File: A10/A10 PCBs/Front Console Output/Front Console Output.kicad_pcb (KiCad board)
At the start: 2 copper layers, 99.8 x 99.5 mm, 43 parts, among them J1 STEPPER_9, J10 STEPPER_5, J11 STEPPER_6, J13 STEPPER_7, J17 STEPPER_8, J2 STEPPER_1, J20 8_MS2, J24 STEPPER_10, J25 STEPPER_11, J26 STEPPER_12, J27 STEPPER_13, J3 STEPPER_2, J41 PWM, J42 Communication, J43 Analog, J44 Analog, J45 Power, J5 STEPPER_3, J6 STEPPER_4, J7 STEPPER IN 12-20VDC, P1 Power, P2 Analog, P3 Analog, P4 Digital, P5 PWM, P6 PWM, P7 Communication, P8 PWM, U1 USR-ES1

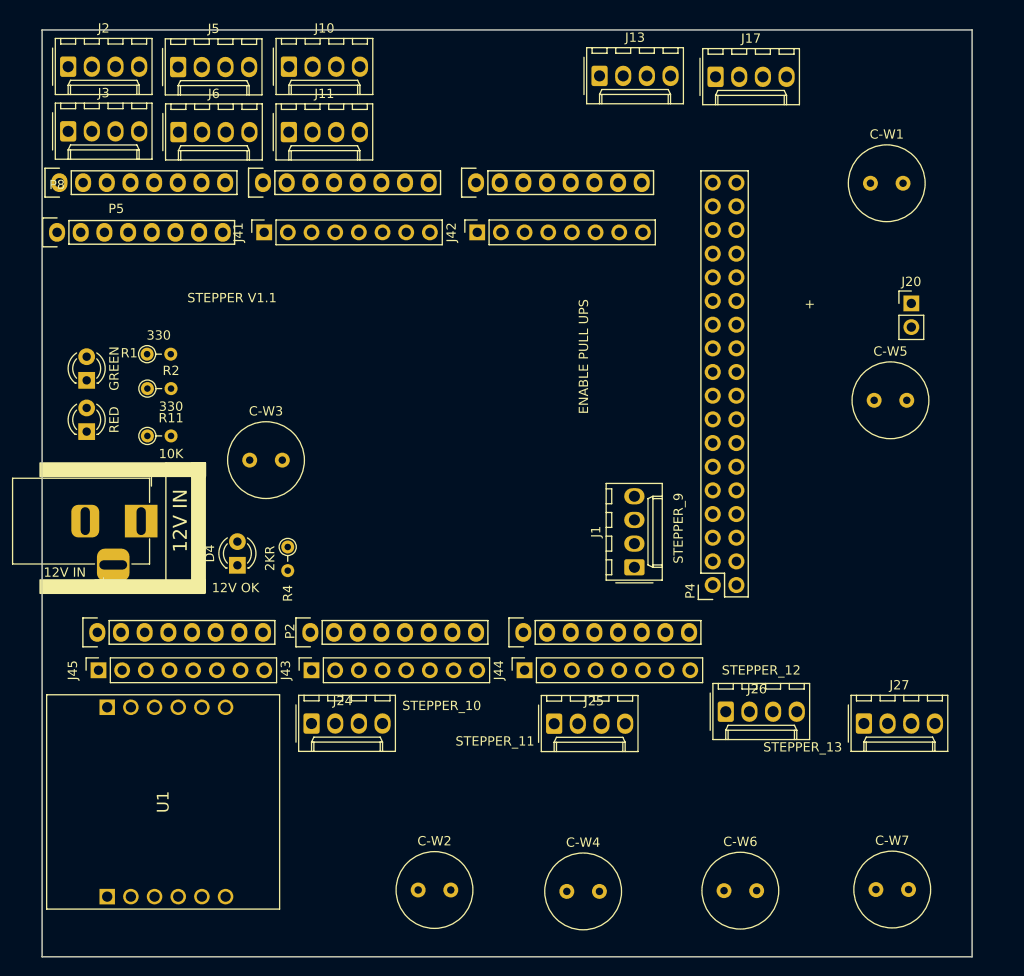
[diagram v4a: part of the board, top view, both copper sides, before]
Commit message: Refreshed Front Console Steppers
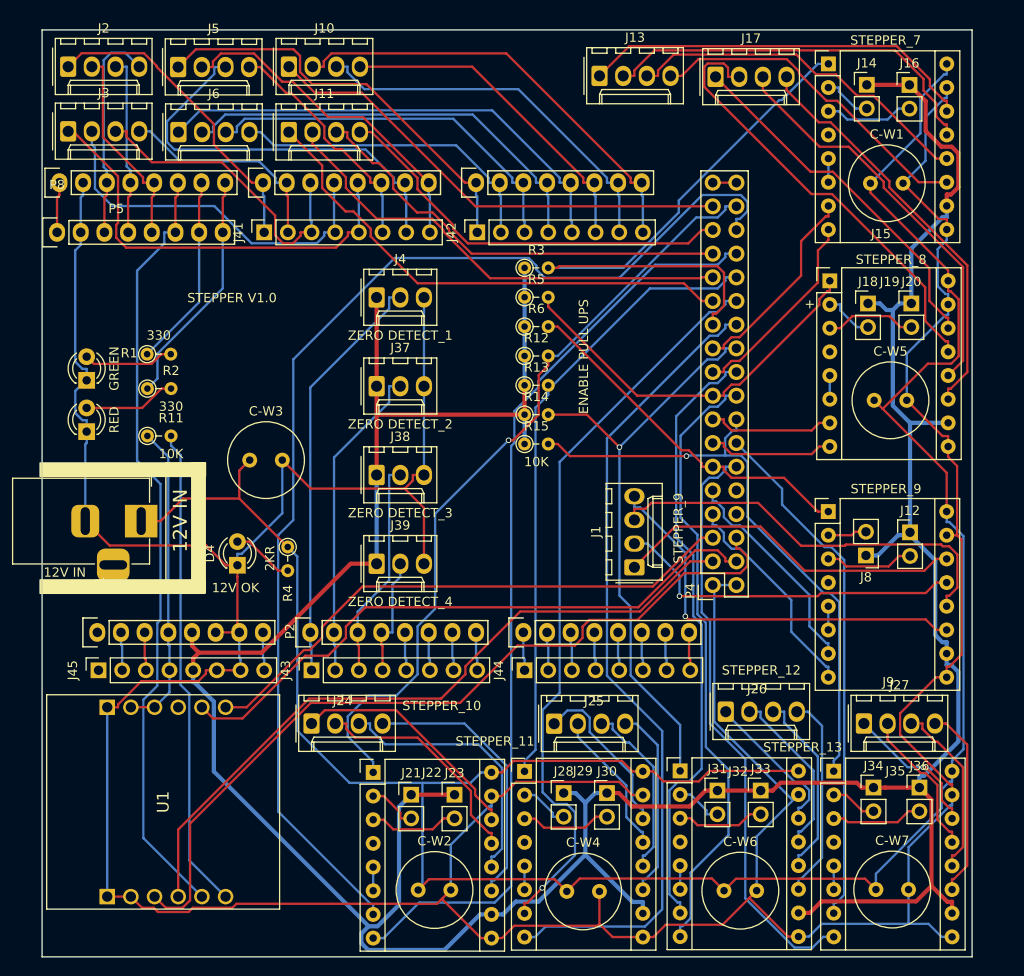
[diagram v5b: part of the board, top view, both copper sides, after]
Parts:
- added J12: 9_MS2, Connector_PinHeader_2.54mm:PinHeader_1x02_P2.54mm_Vertical, F.Cu at (218.5, 108.4)
- added J14: 7_MS1, Connector_PinHeader_2.54mm:PinHeader_1x02_P2.54mm_Vertical, F.Cu at (213.9, 60.4)
- added J15: STEPPER_7, Module:Pololu_Breakout-16_15.2x20.3mm, F.Cu at (209.8, 58.1)
- added J16: 7_MS2, Connector_PinHeader_2.54mm:PinHeader_1x02_P2.54mm_Vertical, F.Cu at (218.5, 60.4)
- added J18: 8_MS1, Connector_PinHeader_2.54mm:PinHeader_1x02_P2.54mm_Vertical, F.Cu at (214.0, 83.8)
- added J19: STEPPER_8, Module:Pololu_Breakout-16_15.2x20.3mm, F.Cu at (209.9, 81.4)
- added J21: 10_MS1, Connector_PinHeader_2.54mm:PinHeader_1x02_P2.54mm_Vertical, F.Cu at (165.0, 136.5)
- added J22: STEPPER_10, Module:Pololu_Breakout-16_15.2x20.3mm, F.Cu at (160.9, 134.2)
- added J23: 10_MS2, Connector_PinHeader_2.54mm:PinHeader_1x02_P2.54mm_Vertical, F.Cu at (169.7, 136.5)
- added J28: 11_MS1, Connector_PinHeader_2.54mm:PinHeader_1x02_P2.54mm_Vertical, F.Cu at (181.4, 136.4)
- added J29: STEPPER_11, Module:Pololu_Breakout-16_15.2x20.3mm, F.Cu at (177.2, 134.0)
- added J30: 11_MS2, Connector_PinHeader_2.54mm:PinHeader_1x02_P2.54mm_Vertical, F.Cu at (186.0, 136.4)
- added J31: 12_MS1, Connector_PinHeader_2.54mm:PinHeader_1x02_P2.54mm_Vertical, F.Cu at (197.9, 136.1)
- added J32: STEPPER_12, Module:Pololu_Breakout-16_15.2x20.3mm, F.Cu at (193.9, 134.0)
- added J33: 12_MS2, Connector_PinHeader_2.54mm:PinHeader_1x02_P2.54mm_Vertical, F.Cu at (202.5, 136.1)
- added J34: 13_MS1, Connector_PinHeader_2.54mm:PinHeader_1x02_P2.54mm_Vertical, F.Cu at (214.6, 135.8)
- added J35: STEPPER_13, Module:Pololu_Breakout-16_15.2x20.3mm, F.Cu at (210.3, 134.0)
- added J36: 13_MS2, Connector_PinHeader_2.54mm:PinHeader_1x02_P2.54mm_Vertical, F.Cu at (219.5, 135.8)
- added J37: ZERO DETECT_2, Connector_Molex:Molex_KK-254_AE-6410-03A_1x03_P2.54mm_Vertical, F.Cu at (161.3, 92.7)
- added J38: ZERO DETECT_3, Connector_Molex:Molex_KK-254_AE-6410-03A_1x03_P2.54mm_Vertical, F.Cu at (161.3, 102.2)
- added J39: ZERO DETECT_4, Connector_Molex:Molex_KK-254_AE-6410-03A_1x03_P2.54mm_Vertical, F.Cu at (161.3, 111.8)
- added J4: ZERO DETECT_1, Connector_Molex:Molex_KK-254_AE-6410-03A_1x03_P2.54mm_Vertical, F.Cu at (161.3, 83.2)
- added J8: 9_MS1, Connector_PinHeader_2.54mm:PinHeader_1x02_P2.54mm_Vertical, F.Cu at (213.8, 110.9)
- added J9: STEPPER_9, Module:Pololu_Breakout-16_15.2x20.3mm, F.Cu at (209.8, 106.2)
- added R12: 10K, Resistor_THT:R_Axial_DIN0204_L3.6mm_D1.6mm_P2.54mm_Vertical, F.Cu at (177.2, 89.5)
- added R13: 10K, Resistor_THT:R_Axial_DIN0204_L3.6mm_D1.6mm_P2.54mm_Vertical, F.Cu at (177.2, 92.6)
- added R14: 10K, Resistor_THT:R_Axial_DIN0204_L3.6mm_D1.6mm_P2.54mm_Vertical, F.Cu at (177.2, 95.8)
- added R15: 10K, Resistor_THT:R_Axial_DIN0204_L3.6mm_D1.6mm_P2.54mm_Vertical, F.Cu at (177.2, 98.9)
- added R3: 10K, Resistor_THT:R_Axial_DIN0204_L3.6mm_D1.6mm_P2.54mm_Vertical, F.Cu at (177.2, 80.0)
- added R5: 10K, Resistor_THT:R_Axial_DIN0204_L3.6mm_D1.6mm_P2.54mm_Vertical, F.Cu at (177.2, 83.2)
- added R6: 10K, Resistor_THT:R_Axial_DIN0204_L3.6mm_D1.6mm_P2.54mm_Vertical, F.Cu at (177.2, 86.3)
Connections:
- net /STEP_V+ renamed /ROLL_STEP_V+
- J10 pad 1: /SCL/21 -> /STEPPER_5_D
- J10 pad 2: /SDA/20 -> /SCL/21
- J10 pad 3: /RX1/19 -> /SDA/20
- J10 pad 4: /STEPPER_5_A -> /RX1/19
- J2 pad 1: /*9 -> /*7
- J3 pad 1: /*4 -> /*3
- J3 pad 2: /*5 -> /*4
- J3 pad 3: /*6 -> /*5
- J3 pad 4: /*7 -> /*6
- J41 pad 7: /STEPPER_3_C -> /STEPPER_3_B
- J42 pad 1: /STEPPER_4_A -> /STEPPER_3_D
- J42 pad 3: /STEPPER_4_C -> /STEPPER_4_B
- J42 pad 5: /STEPPER_5_A -> /STEPPER_4_D
- J5 pad 1: /RX0/0 -> /STEPPER_3_D
- J5 pad 2: /STEPPER_3_C -> /RX0/0
- J5 pad 3: /*2 -> /STEPPER_3_B
- J5 pad 4: /*3 -> /*2
- J6 pad 1: /RX2/17 -> /STEPPER_4_D
- J6 pad 2: /STEPPER_4_C -> /RX2/17
- J6 pad 3: /RX3/15 -> /STEPPER_4_B
- J6 pad 4: /STEPPER_4_A -> /RX3/15
- P4 pad 10: /STEPPER_11_A -> unconnected-(P4-Pin_10-Pad10)
- P4 pad 11: /STEPPER_8_D -> /9_EN
- P4 pad 12: /STEPPER_11_D -> /13_DIR
- P4 pad 13: /STEPPER_8_C -> /8_DIR
- P4 pad 14: /STEPPER_11_C -> /13_STEP
- P4 pad 15: /STEPPER_8_B -> /8_STEP
- P4 pad 16: /STEPPER_11_B -> /13_EN
- P4 pad 17: /STEPPER_8_A -> /8_EN
- P4 pad 18: /STEPPER_11_A -> /12_DIR
- P4 pad 19: /STEPPER_7_D -> /7_DIR
- P4 pad 20: /STEPPER_10_D -> /12_STEP
- P4 pad 21: /STEPPER_7_C -> /7_STEP
- P4 pad 22: /STEPPER_10_C -> /12_EN
- P4 pad 23: /STEPPER_7_B -> /7_EN
- P4 pad 24: /STEPPER_10_B -> /11_DIR
- P4 pad 25: /STEPPER_7_A -> /STEPPER_6_D
- P4 pad 26: /STEPPER_10_A -> /11_STEP
- P4 pad 27: /STEPPER_6_D -> /STEPPER_6_C
- P4 pad 28: /STEPPER_9_D -> /11_EN
- P4 pad 29: /STEPPER_6_C -> /STEPPER_6_B
- P4 pad 30: /STEPPER_9_C -> /10_DIR
- P4 pad 31: /STEPPER_6_B -> /STEPPER_6_A
- P4 pad 32: /STEPPER_9_B -> /10_STEP
- P4 pad 33: /STEPPER_6_A -> /STEPPER_5_D
- P4 pad 34: /STEPPER_9_A -> /10_EN
- P4 pad 7: /STEPPER_11_D -> /9_DIR
- P4 pad 8: /STEPPER_11_B -> unconnected-(P4-Pin_8-Pad8)
- P4 pad 9: /STEPPER_11_C -> /9_STEP
- P6 pad 7: /STEPPER_3_C -> /STEPPER_3_B
- P7 pad 1: /STEPPER_4_A -> /STEPPER_3_D
- P7 pad 3: /STEPPER_4_C -> /STEPPER_4_B
- P7 pad 5: /STEPPER_5_A -> /STEPPER_4_D
- R1 pad 1: /GREEN_LED -> /*9
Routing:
- net GND: track 0.00 -> 452.2 mm
- net +5VL: track 0.00 -> 370.1 mm
- net /ROLL_STEP_V+: track 0.00 -> 276.2 mm
- net /10_STEP: track 0.00 -> 126.7 mm
- net /10_DIR: track 0.00 -> 99.6 mm
- net MOSI: track 0.00 -> 88.6 mm
- net /11_DIR: track 0.00 -> 88.2 mm
- net /10_EN: track 0.00 -> 83.8 mm, vias 0 -> 1
- net SS: track 0.00 -> 83.5 mm
- net /11_STEP: track 0.00 -> 80.2 mm, vias 0 -> 1
- net SCLK: track 0.00 -> 77.0 mm
- net /11_EN: track 0.00 -> 67.9 mm
- net ES1_RST: track 0.00 -> 66.7 mm
- net /12_DIR: track 0.00 -> 66.2 mm
- net /12_STEP: track 0.00 -> 65.8 mm
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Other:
- board text added: "STEPPER V1.0"
- board text removed: "STEPPER V1.1"
